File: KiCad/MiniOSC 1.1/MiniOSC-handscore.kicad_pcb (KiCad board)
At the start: 2 copper layers, 90.1 x 128.5 mm, 58 parts, among them J1 Conn_01x16_Female, J2 Conn_01x16_Male, J3 V_OCT_IN, J4 FM_IN, J5 PULSE_OUT, J6 SAW_OUT, J7 JST_BUS, J8 IDC_BUS, Q1 BC558, Q2 BC548, U1 TL074, U2 40106

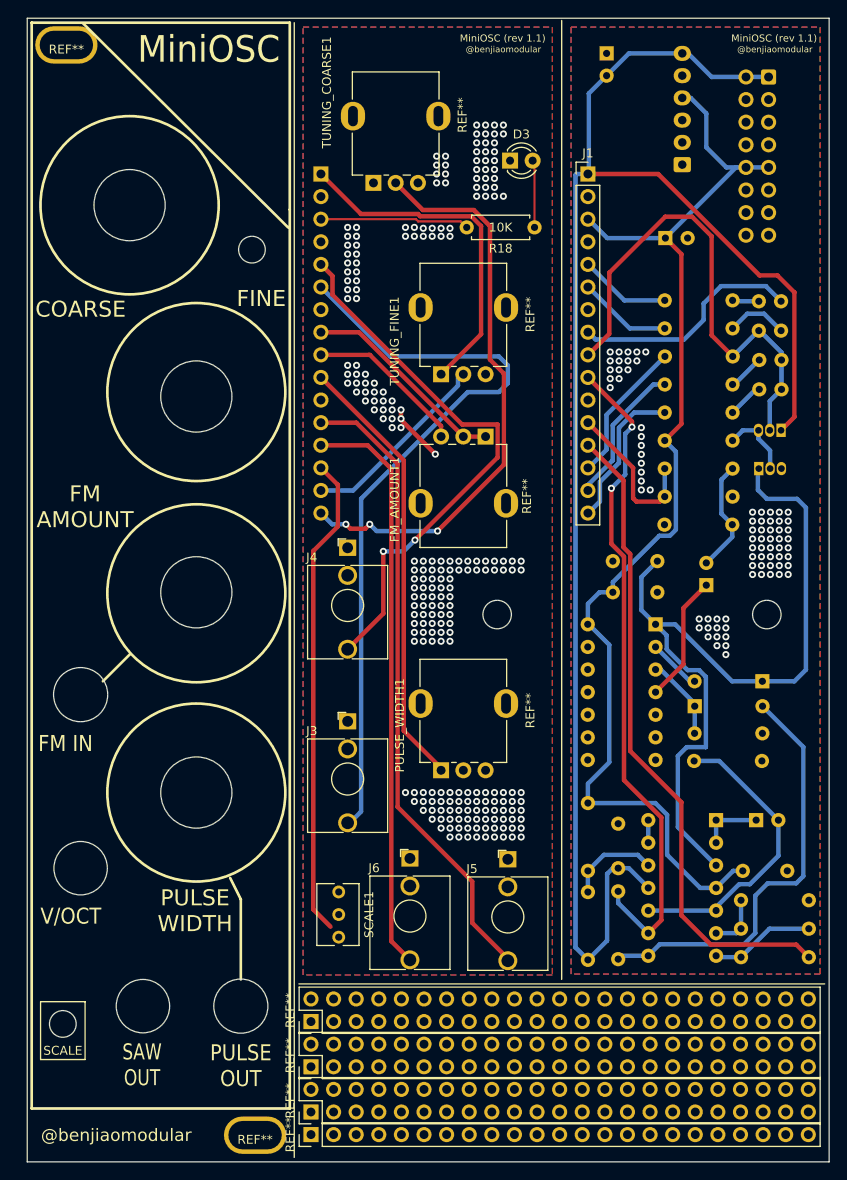
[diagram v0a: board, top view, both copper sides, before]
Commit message: fixing traces on fine tuning 1.1 and 1.1 handscore
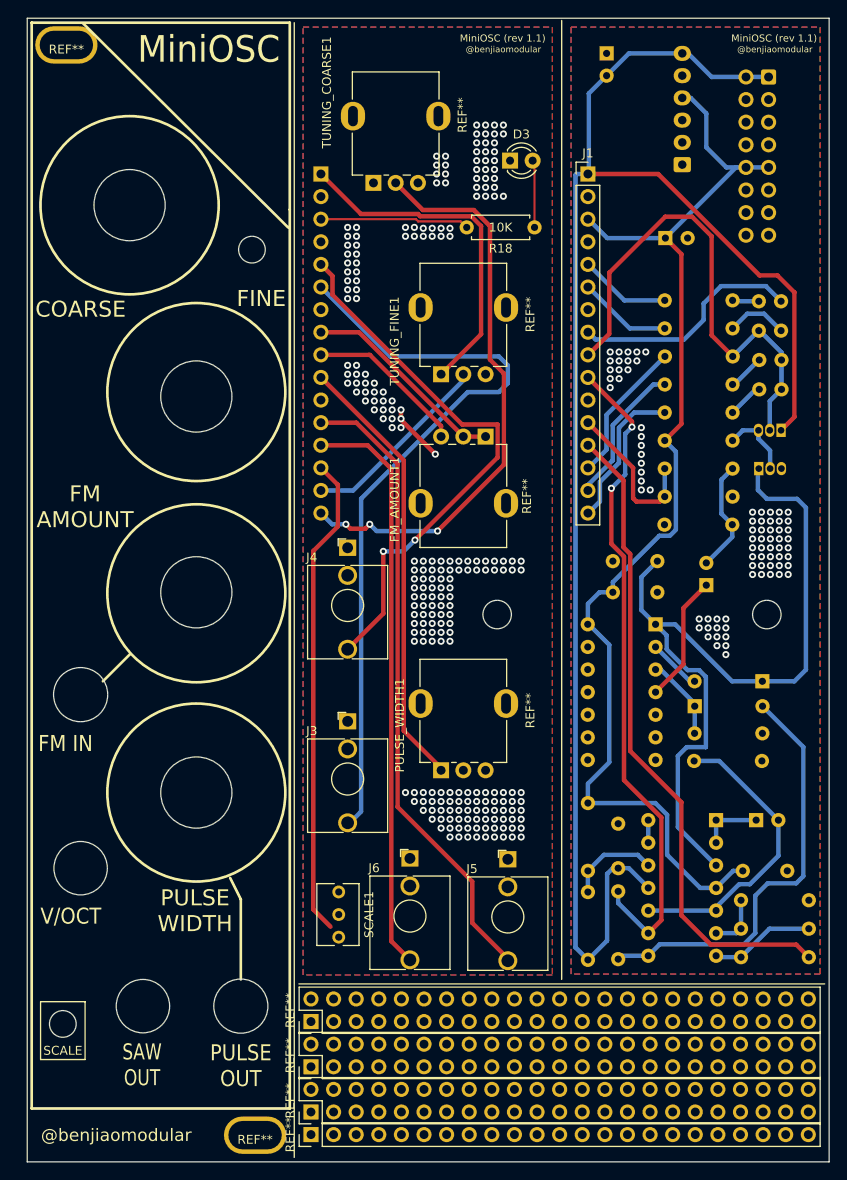
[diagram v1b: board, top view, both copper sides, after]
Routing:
- net FP_12V_NEG: track 39.4 -> 38.9 mm
